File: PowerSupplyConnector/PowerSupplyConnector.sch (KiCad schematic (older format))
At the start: 2 parts

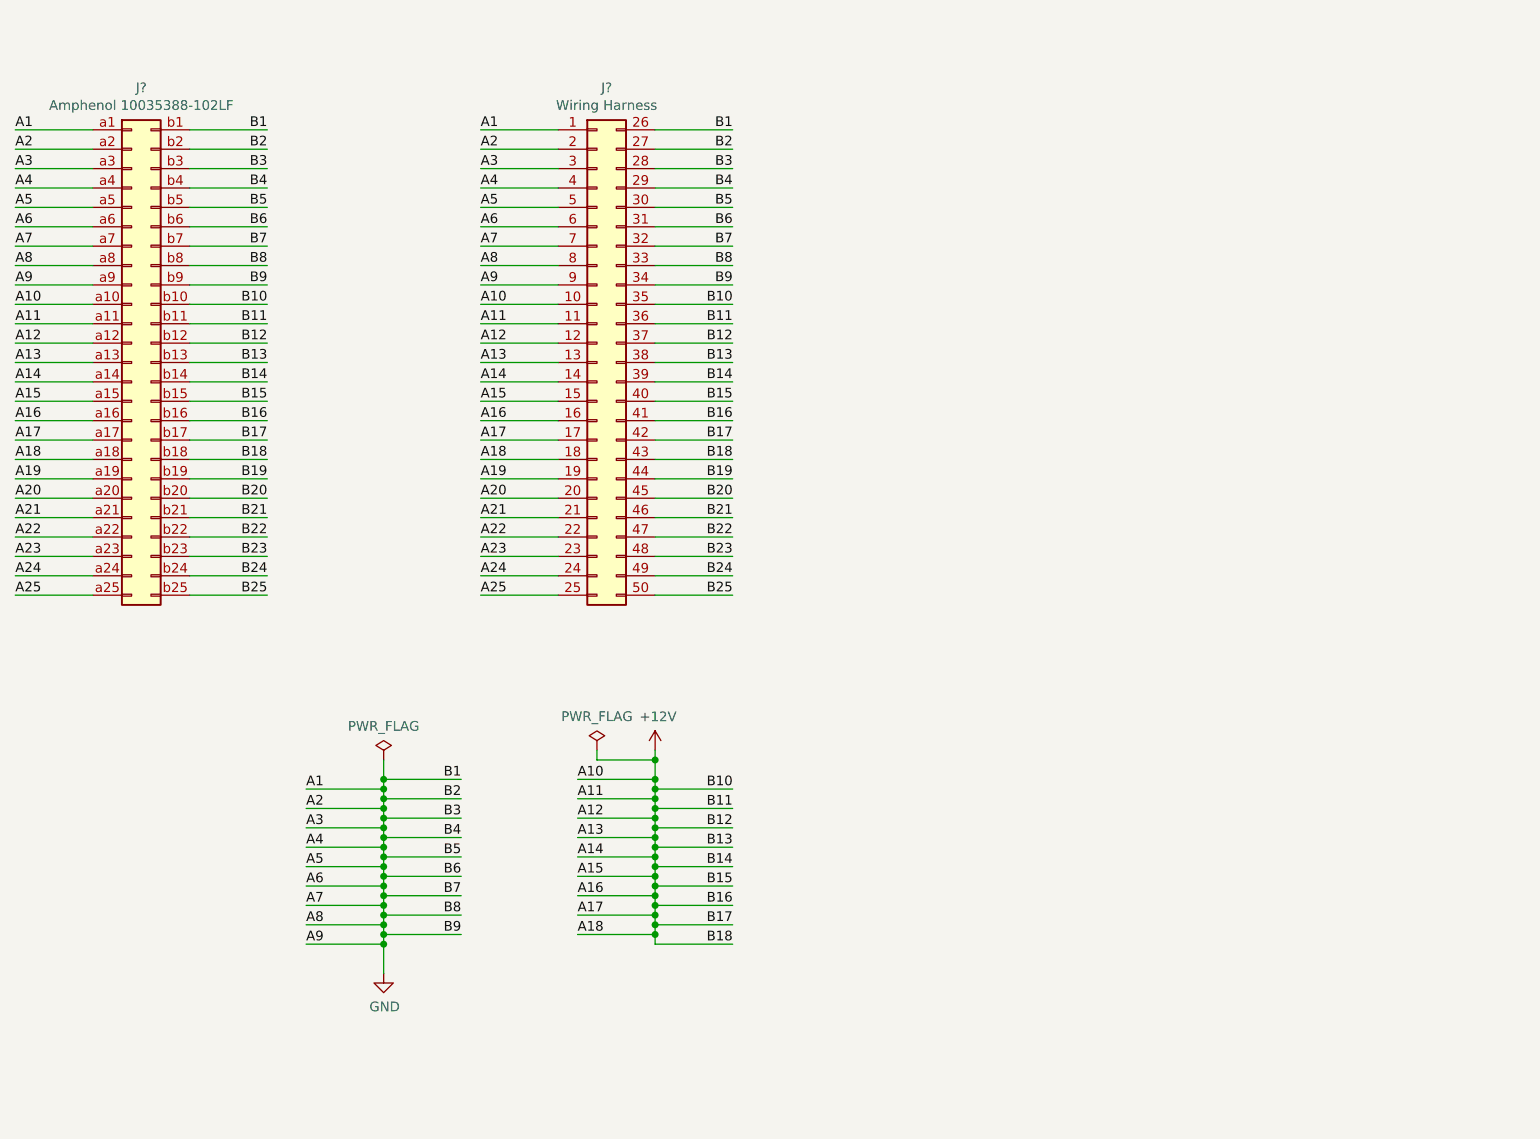
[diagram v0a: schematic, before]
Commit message: change to terminal block connector
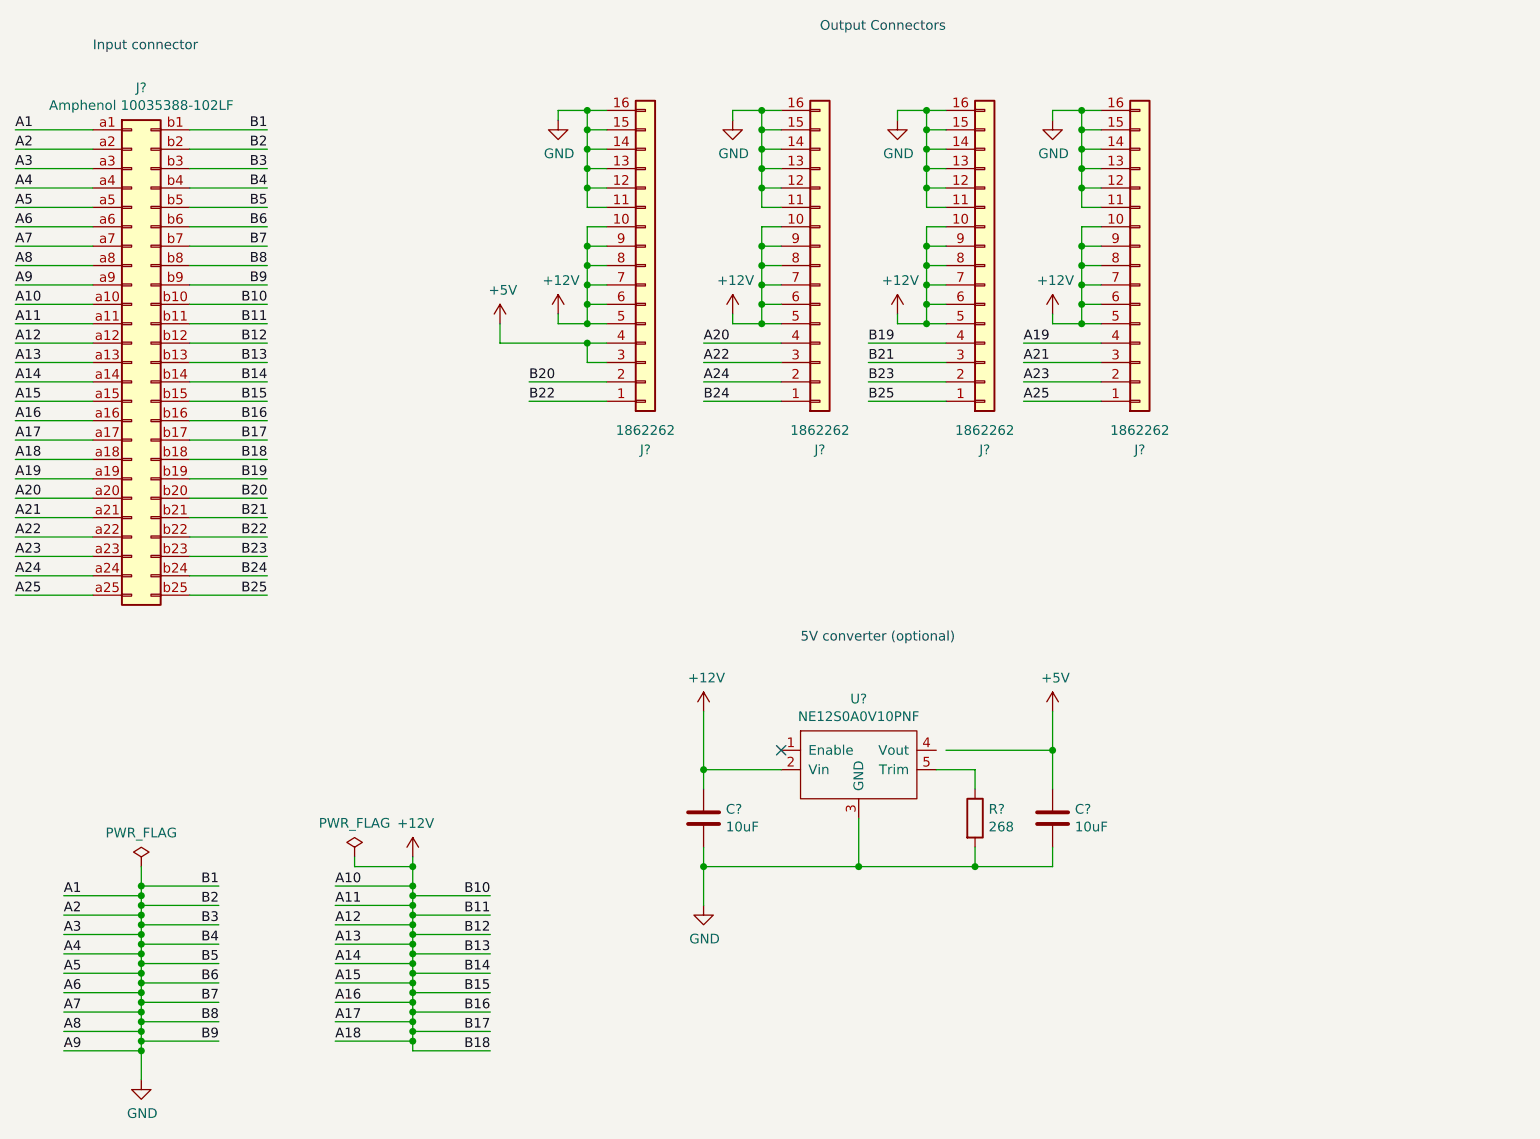
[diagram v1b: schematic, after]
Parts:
- removed J?: Wiring Harness, symbol Connector_Generic:Conn_02x25_Top_Bottom
- added C? (x2): 10uF, symbol Device:C
- added J? (x4): 1862262, symbol Connector_Generic:Conn_01x16
- added R?: 268, symbol Device:R
- added U?: NE12S0A0V10PNF, symbol NE12S0A0V10PNF:NE12S0A0V10PNF
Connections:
- net +12V: now also C?.1, J?.10 (Pin_10), J?.10 (Pin_10), J?.10 (Pin_10), J?.10 (Pin_10), J?.5 (Pin_5), J?.5 (Pin_5), J?.5 (Pin_5), J?.5 (Pin_5), J?.6 (Pin_6), J?.6 (Pin_6), J?.6 (Pin_6), J?.6 (Pin_6), J?.7 (Pin_7), J?.7 (Pin_7), J?.7 (Pin_7), J?.7 (Pin_7), J?.8 (Pin_8), J?.8 (Pin_8), J?.8 (Pin_8), J?.8 (Pin_8), J?.9 (Pin_9), J?.9 (Pin_9), J?.9 (Pin_9), J?.9 (Pin_9), U?.2 (Vin)
- net A19: now also J?.4 (Pin_4)
- net A20: now also J?.4 (Pin_4)
- net A21: now also J?.3 (Pin_3)
- net A22: now also J?.3 (Pin_3)
- net A23: now also J?.2 (Pin_2)
- net A24: now also J?.2 (Pin_2)
- net A25: now also J?.1 (Pin_1)
- net B19: now also J?.4 (Pin_4)
- net B20: now also J?.2 (Pin_2)
- net B21: now also J?.3 (Pin_3)
- net B22: now also J?.1 (Pin_1)
- net B23: now also J?.2 (Pin_2)
- net B24: now also J?.1 (Pin_1)
- net B25: now also J?.1 (Pin_1)
- net GND: now also C?.2, C?.2, J?.11 (Pin_11), J?.11 (Pin_11), J?.11 (Pin_11), J?.11 (Pin_11), J?.12 (Pin_12), J?.12 (Pin_12), J?.12 (Pin_12), J?.12 (Pin_12), J?.13 (Pin_13), J?.13 (Pin_13), J?.13 (Pin_13), J?.13 (Pin_13), J?.14 (Pin_14), J?.14 (Pin_14), J?.14 (Pin_14), J?.14 (Pin_14), J?.15 (Pin_15), J?.15 (Pin_15), J?.15 (Pin_15), J?.15 (Pin_15), J?.16 (Pin_16), J?.16 (Pin_16), J?.16 (Pin_16), J?.16 (Pin_16), R?.2, U?.3 (GND)
- new net: R?.1, U?.5 (Trim)
- new net +5V: C?.1, J?.3 (Pin_3), J?.4 (Pin_4)
- no-connect marks 0 -> 1
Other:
- note added: "5V converter (optional)"
- note added: "Input connector"
- note added: "Output Connectors"

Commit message: first draft of pcb for power supply side
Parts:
- added H1, H2, H3, H4: M3, MountingHole:MountingHole_3.2mm_M3_Pad, symbol Mechanical:MountingHole_Pad
- C1, C2: renamed from C?; footprint (none) -> Capacitor_SMD:C_0603_1608Metric
- J1: renamed from J?; footprint (none) -> SupermicroConnectors:Amphenol_10035388-102LF
- J2, J3, J4, J5: renamed from J?; footprint (none) -> PhoenixContact:PhoenixContact1862262
- R1: renamed from R?; footprint (none) -> Resistor_SMD:R_0603_1608Metric
- U1: renamed from U?; value NE12S0A0V10PNF -> NE12S0A0V10; footprint (none) -> Delta:Delta_NE12S0A0V10
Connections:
- net +5V: now also U1.4 (Vout)
- net GND: now also H1.1, H2.1, H3.1, H4.1
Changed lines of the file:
@@
 $EndDescr
 $Comp
-L Connector_Generic:Conn_02x25_Row_Letter_First J?
+L Connector_Generic:Conn_02x25_Row_Letter_First J1
 U 1 1 5C0D7C6F
 P 2750 3000
-F 0 "J?" H 2800 4417 50  0000 C CNN
+F 0 "J1" H 2800 4417 50  0000 C CNN
 F 1 "Amphenol 10035388-102LF" H 2800 4326 50  0000 C CNN
-F 2 "" H 2750 3000 50  0001 C CNN
+F 2 "SupermicroConnectors:Amphenol_10035388-102LF" H 2750 3000 50  0001 C CNN
 F 3 "~" H 2750 3000 50  0001 C CNN
 	1    2750 3000
@@
 	4200 6450 4200 6500
 $Comp
-L Connector_Generic:Conn_01x16 J?
+L Connector_Generic:Conn_01x16 J2
 U 1 1 5C17DCF5
 P 5400 2500
-F 0 "J?" H 5400 3450 50  0000 C CNN
+F 0 "J2" H 5400 3450 50  0000 C CNN
 F 1 "1862262" H 5400 3350 50  0000 C CNN
-F 2 "" H 5400 2500 50  0001 C CNN
+F 2 "PhoenixContact:PhoenixContact1862262" H 5400 2500 50  0001 C CNN
 F 3 "~" H 5400 2500 50  0001 C CNN
 	1    5400 2500
@@
 $EndComp
 $Comp
-L Connector_Generic:Conn_01x16 J?
+L Connector_Generic:Conn_01x16 J3
 U 1 1 5C17DD8D
 P 6300 2500
-F 0 "J?" H 6300 3450 50  0000 C CNN
+F 0 "J3" H 6300 3450 50  0000 C CNN
 F 1 "1862262" H 6300 3350 50  0000 C CNN
-F 2 "" H 6300 2500 50  0001 C CNN
+F 2 "PhoenixContact:PhoenixContact1862262" H 6300 2500 50  0001 C CNN
 F 3 "~" H 6300 2500 50  0001 C CNN
 	1    6300 2500
@@
 $EndComp
 $Comp
-L Connector_Generic:Conn_01x16 J?
+L Connector_Generic:Conn_01x16 J4
 U 1 1 5C17DDDA
 P 7150 2500
-F 0 "J?" H 7150 3450 50  0000 C CNN
+F 0 "J4" H 7150 3450 50  0000 C CNN
 F 1 "1862262" H 7150 3350 50  0000 C CNN
-F 2 "" H 7150 2500 50  0001 C CNN
+F 2 "PhoenixContact:PhoenixContact1862262" H 7150 2500 50  0001 C CNN
 F 3 "~" H 7150 2500 50  0001 C CNN
 	1    7150 2500
@@
 $EndComp
 $Comp
-L Connector_Generic:Conn_01x16 J?
+L Connector_Generic:Conn_01x16 J5
 U 1 1 5C17DE4E
 P 7950 2500
-F 0 "J?" H 7950 3450 50  0000 C CNN
+F 0 "J5" H 7950 3450 50  0000 C CNN
 F 1 "1862262" H 7950 3350 50  0000 C CNN
-F 2 "" H 7950 2500 50  0001 C CNN
+F 2 "PhoenixContact:PhoenixContact1862262" H 7950 2500 50  0001 C CNN
 F 3 "~" H 7950 2500 50  0001 C CNN
 	1    7950 2500
@@
 	5200 3200 4800 3200
 $Comp
-L NE12S0A0V10PNF:NE12S0A0V10PNF U?
+L NE12S0A0V10PNF:NE12S0A0V10PNF U1
 U 1 1 5C4F45DB
 P 6500 5300
-F 0 "U?" H 6500 5865 50  0000 C CNN
-F 1 "NE12S0A0V10PNF" H 6500 5774 50  0000 C CNN
-F 2 "" H 6500 5300 50  0001 C CNN
+F 0 "U1" H 6500 5865 50  0000 C CNN
+F 1 "NE12S0A0V10" H 6500 5774 50  0000 C CNN
+F 2 "Delta:Delta_NE12S0A0V10" H 6500 5300 50  0001 C CNN
 F 3 "" H 6500 5300 50  0001 C CNN
 	1    6500 5300
@@
 $EndComp
 $Comp
-L Device:R R?
+L Device:R R1
 U 1 1 5C50E3E1
 P 7100 5350
-F 0 "R?" H 7170 5396 50  0000 L CNN
+F 0 "R1" H 7170 5396 50  0000 L CNN
 F 1 "268" H 7170 5305 50  0000 L CNN
-F 2 "" V 7030 5350 50  0001 C CNN
+F 2 "Resistor_SMD:R_0603_1608Metric" V 7030 5350 50  0001 C CNN
 F 3 "~" H 7100 5350 50  0001 C CNN
 	1    7100 5350
@@
 $EndComp
 $Comp
-L Device:C C?
+L Device:C C2
 U 1 1 5C50E459
 P 7500 5350
-F 0 "C?" H 7615 5396 50  0000 L CNN
+F 0 "C2" H 7615 5396 50  0000 L CNN
 F 1 "10uF" H 7615 5305 50  0000 L CNN
-F 2 "" H 7538 5200 50  0001 C CNN
+F 2 "Capacitor_SMD:C_0603_1608Metric" H 7538 5200 50  0001 C CNN
 F 3 "~" H 7500 5350 50  0001 C CNN
 	1    7500 5350
@@
 $EndComp
 $Comp
-L Device:C C?
+L Device:C C1
 U 1 1 5C50E64A
 P 5700 5350
-F 0 "C?" H 5815 5396 50  0000 L CNN
+F 0 "C1" H 5815 5396 50  0000 L CNN
 F 1 "10uF" H 5815 5305 50  0000 L CNN
-F 2 "" H 5738 5200 50  0001 C CNN
+F 2 "Capacitor_SMD:C_0603_1608Metric" H 5738 5200 50  0001 C CNN
 F 3 "~" H 5700 5350 50  0001 C CNN
 	1    5700 5350
@@
 Wire Wire Line
 	7100 5100 7100 5200
-Wire Wire Line
-	6950 5000 7500 5000
 Wire Wire Line
 	7500 5000 7500 4800
@@
 	5700 5600 5700 5800
 Connection ~ 5700 5600
+Wire Wire Line
+	6900 5000 7500 5000
+$Comp
+L Mechanical:MountingHole_Pad H1
+U 1 1 5C1870CC
+P 8800 4100
+F 0 "H1" H 8900 4151 50  0000 L CNN
+F 1 "M3" H 8900 4060 50  0000 L CNN
+F 2 "MountingHole:MountingHole_3.2mm_M3_Pad" H 8800 4100 50  0001 C CNN
+F 3 "~" H 8800 4100 50  0001 C CNN
+	1    8800 4100
+	1    0    0    -1
+$EndComp
+$Comp
+L Mechanical:MountingHole_Pad H2
+U 1 1 5C1871C6
+P 9100 4100
+F 0 "H2" H 9200 4151 50  0000 L CNN
+F 1 "M3" H 9200 4060 50  0000 L CNN
+F 2 "MountingHole:MountingHole_3.2mm_M3_Pad" H 9100 4100 50  0001 C CNN
+F 3 "~" H 9100 4100 50  0001 C CNN
+	1    9100 4100
+	1    0    0    -1
+$EndComp
+$Comp
+L Mechanical:MountingHole_Pad H3
+U 1 1 5C18726C
+P 9400 4100
+F 0 "H3" H 9500 4151 50  0000 L CNN
+F 1 "M3" H 9500 4060 50  0000 L CNN
+F 2 "MountingHole:MountingHole_3.2mm_M3_Pad" H 9400 4100 50  0001 C CNN
+F 3 "~" H 9400 4100 50  0001 C CNN
+	1    9400 4100
+	1    0    0    -1
+$EndComp
+$Comp
+L Mechanical:MountingHole_Pad H4
+U 1 1 5C1872D8
+P 9700 4100
+F 0 "H4" H 9800 4151 50  0000 L CNN
+F 1 "M3" H 9800 4060 50  0000 L CNN
+F 2 "MountingHole:MountingHole_3.2mm_M3_Pad" H 9700 4100 50  0001 C CNN
+F 3 "~" H 9700 4100 50  0001 C CNN
+	1    9700 4100
+	1    0    0    -1
+$EndComp
+$Comp
+L power:GND #PWR0115
+U 1 1 5C19698B
+P 9250 4400
+F 0 "#PWR0115" H 9250 4150 50  0001 C CNN
+F 1 "GND" H 9255 4227 50  0000 C CNN
+F 2 "" H 9250 4400 50  0001 C CNN
+F 3 "" H 9250 4400 50  0001 C CNN
+	1    9250 4400
+	1    0    0    -1
+$EndComp
+Wire Wire Line
+	8800 4200 8800 4300
+Wire Wire Line
+	8800 4300 9100 4300
+Wire Wire Line
+	9250 4300 9250 4400
+Wire Wire Line
+	9100 4200 9100 4300
+Connection ~ 9100 4300
+Wire Wire Line
+	9100 4300 9250 4300
+Wire Wire Line
+	9400 4200 9400 4300
+Wire Wire Line
+	9400 4300 9250 4300
+Connection ~ 9250 4300
+Wire Wire Line
+	9700 4200 9700 4300
+Wire Wire Line
+	9700 4300 9400 4300
+Connection ~ 9400 4300
 $EndSCHEMATC
